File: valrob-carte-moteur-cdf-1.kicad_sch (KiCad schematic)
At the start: 50 parts, among them J1 USB_C_Receptacle_USB2.0_14P, J2 Conn_01x02, J3 Conn_01x02, J4 Conn_01x04_Pin, J5 Conn_01x08, J6 Conn_01x02, J7 Conn_01x02, J8 Conn_01x08, J9 Conn_01x04_Pin, SW1 SW_Push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

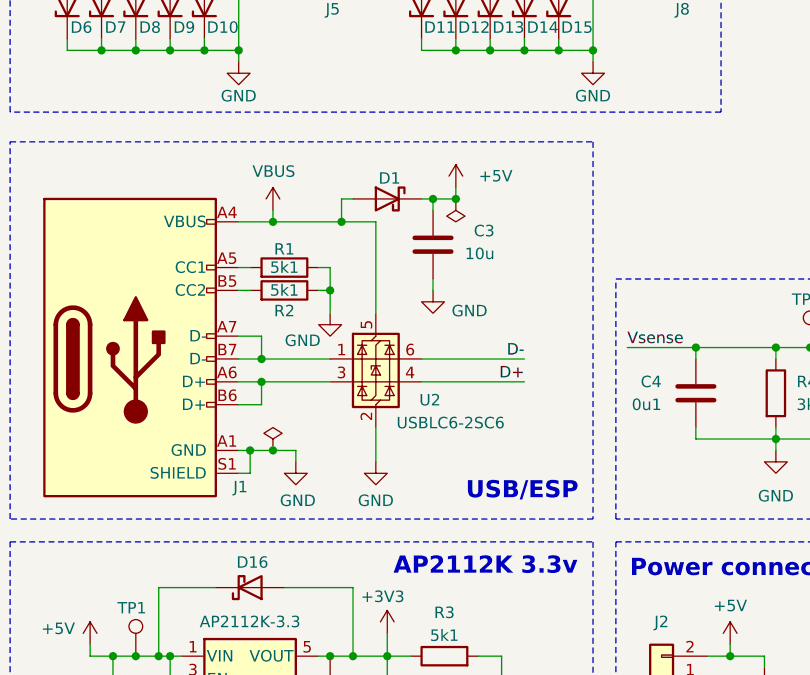
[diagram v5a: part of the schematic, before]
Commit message: switch ST usb ESD to H5VU10U tvs diodes
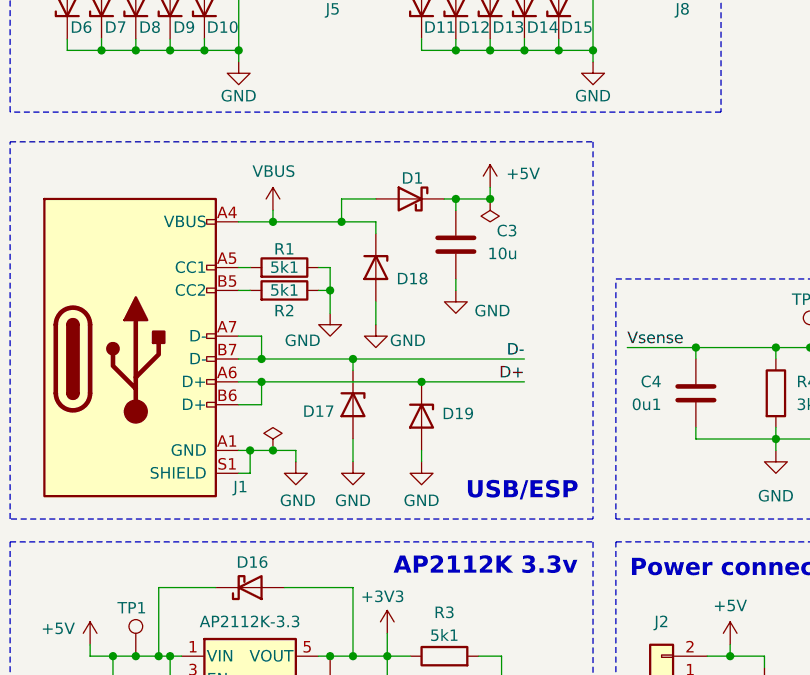
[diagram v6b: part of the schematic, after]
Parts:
- removed U2: USBLC6-2SC6, Package_TO_SOT_SMD:SOT-23-6, symbol Power_Protection:USBLC6-2SC6
- added D17, D18, D19: H5VU10U, Pers:Diode_DFN1006, symbol Pers:H5VU10U
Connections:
- net D+: now also J1.A6 (D+), J1.B6 (D+), D19.1 (K)
- net D-: now also J1.A7 (D-), J1.B7 (D-), D17.1 (K)
- net GND: now also D17.2 (A), D18.2 (A), D19.2 (A)
- net VBUS: now also D18.1 (K)
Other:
- moved on the sheet: C3, D1

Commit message: pcb(silkscreeen): improvements
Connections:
- net +12V: now also C4.1, D4.1 (K), TP3.1
- net Vsense: no longer C4.1, D4.1 (K), TP3.1
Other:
- moved on the sheet: C4, D4, R4, R6, TP3

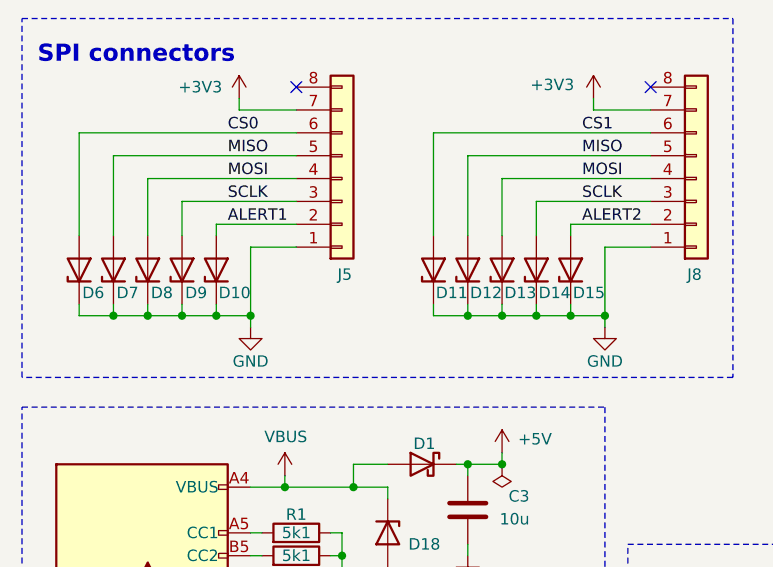
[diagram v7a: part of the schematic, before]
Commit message: fix spi connectors TVS diodes polarity
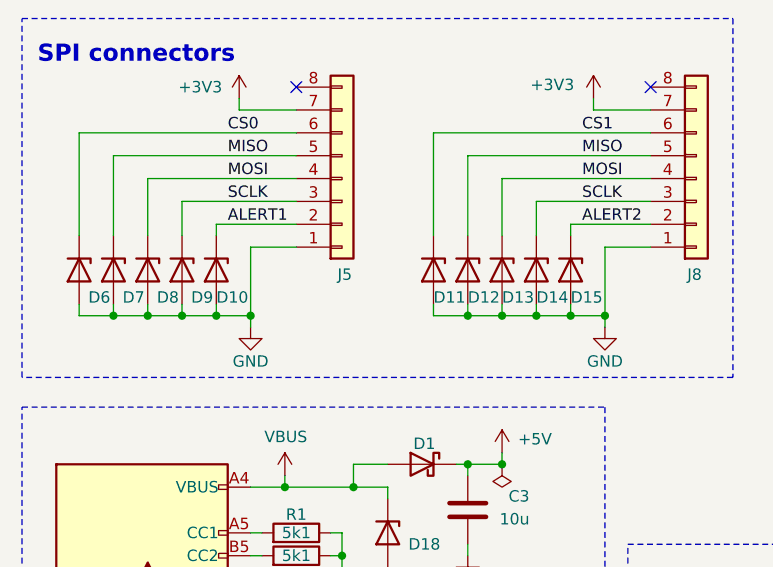
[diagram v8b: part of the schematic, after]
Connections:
- net ALERT1: now also D10.1 (K); no longer D10.2 (A)
- net ALERT2: now also D15.1 (K); no longer D15.2 (A)
- net CS0: now also D6.1 (K); no longer D6.2 (A)
- net CS1: now also D11.1 (K); no longer D11.2 (A)
- net GND: now also D10.2 (A), D11.2 (A), D12.2 (A), D13.2 (A), D14.2 (A), D15.2 (A), D6.2 (A), D7.2 (A), D8.2 (A), D9.2 (A); no longer D10.1 (K), D11.1 (K), D12.1 (K), D13.1 (K), D14.1 (K), D15.1 (K), D6.1 (K), D7.1 (K), D8.1 (K), D9.1 (K)
- net MISO: now also D12.1 (K), D7.1 (K); no longer D12.2 (A), D7.2 (A)
- net MOSI: now also D13.1 (K), D8.1 (K); no longer D13.2 (A), D8.2 (A)
- net SCLK: now also D14.1 (K), D9.1 (K); no longer D14.2 (A), D9.2 (A)
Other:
- moved on the sheet: D10, D11, D12, D13, D14, D15, D6, D7, D8, D9
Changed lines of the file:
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@@
 	(wire
 		(pts
-			(xy 40.64 102.87) (xy 40.64 110.49)
-		)
-		(stroke
-			(width 0)
-			(type default)
-		)
-	)
-	(wire
-		(pts
 			(xy 55.88 129.54) (xy 52.07 129.54)
 		)
@@
 	(wire
 		(pts
+			(xy 40.64 102.87) (xy 40.64 110.49)
+		)
+		(stroke
+			(width 0)
+			(type default)
+		)
+	)
+	(wire
+		(pts
 			(xy 26.67 187.96) (xy 26.67 189.23)
 		)
@@
 	(symbol
 		(lib_id "Pers:H5VU10U")
-		(at 68.58 105.41 90)
+		(at 68.58 105.41 270)
 		(unit 1)
 		(exclude_from_sim no)
@@
 		(dnp no)
 		(property "Reference" "D13"
-			(at 72.39 107.95 90)
+			(at 68.58 108.458 90)
 			(effects
 				(font
@@
 		)
 		(property "Value" "H5VU10U"
-			(at 66.04 104.1401 90)
+			(at 71.12 106.6799 90)
 			(effects
 				(font
@@
 		)
 		(property "Footprint" "Pers:Diode_DFN1006"
-			(at 73.025 105.41 0)
+			(at 64.135 105.41 0)
 			(effects
 				(font
@@
 	(symbol
 		(lib_id "Pers:H5VU10U")
-		(at 21.59 105.41 90)
+		(at 21.59 105.41 270)
 		(unit 1)
 		(exclude_from_sim no)
@@
 		(dnp no)
 		(property "Reference" "D6"
-			(at 24.384 107.95 90)
+			(at 22.606 108.458 90)
 			(effects
 				(font
@@
 		)
 		(property "Value" "H5VU10U"
-			(at 19.05 104.1401 90)
+			(at 24.13 106.6799 90)
 			(effects
 				(font
@@
 		)
 		(property "Footprint" "Pers:Diode_DFN1006"
-			(at 26.035 105.41 0)
+			(at 17.145 105.41 0)
 			(effects
 				(font
@@
 	(symbol
 		(lib_id "Pers:H5VU10U")
-		(at 64.77 105.41 90)
+		(at 64.77 105.41 270)
 		(unit 1)
 		(exclude_from_sim no)
@@
 		(dnp no)
 		(property "Reference" "D12"
-			(at 68.58 107.95 90)
+			(at 64.77 108.458 90)
 			(effects
 				(font
@@
 		)
 		(property "Value" "H5VU10U"
-			(at 62.23 104.1401 90)
+			(at 67.31 106.6799 90)
 			(effects
 				(font
@@
 		)
 		(property "Footprint" "Pers:Diode_DFN1006"
-			(at 69.215 105.41 0)
+			(at 60.325 105.41 0)
 			(effects
 				(font
@@
 	(symbol
 		(lib_id "Pers:H5VU10U")
-		(at 29.21 105.41 90)
+		(at 29.21 105.41 270)
 		(unit 1)
 		(exclude_from_sim no)
@@
 		(dnp no)
 		(property "Reference" "D8"
-			(at 32.004 107.95 90)
+			(at 30.226 108.458 90)
 			(effects
 				(font
@@
 		)
 		(property "Value" "H5VU10U"
-			(at 26.67 104.1401 90)
+			(at 31.75 106.6799 90)
 			(effects
 				(font
@@
 		)
 		(property "Footprint" "Pers:Diode_DFN1006"
-			(at 33.655 105.41 0)
+			(at 24.765 105.41 0)
 			(effects
 				(font
@@
 	(symbol
 		(lib_id "Pers:H5VU10U")
-		(at 25.4 105.41 90)
+		(at 25.4 105.41 270)
 		(unit 1)
 		(exclude_from_sim no)
@@
 		(dnp no)
 		(property "Reference" "D7"
-			(at 28.194 107.95 90)
+			(at 26.416 108.458 90)
 			(effects
 				(font
@@
 		)
 		(property "Value" "H5VU10U"
-			(at 22.86 104.1401 90)
+			(at 27.94 106.6799 90)
 			(effects
 				(font
@@
 		)
 		(property "Footprint" "Pers:Diode_DFN1006"
-			(at 29.845 105.41 0)
+			(at 20.955 105.41 0)
 			(effects
 				(font
@@
 	(symbol
 		(lib_id "Pers:H5VU10U")
-		(at 33.02 105.41 90)
+		(at 33.02 105.41 270)
 		(unit 1)
 		(exclude_from_sim no)
@@
 		(dnp no)
 		(property "Reference" "D9"
-			(at 35.814 107.95 90)
+			(at 34.036 108.458 90)
 			(effects
 				(font
@@
 		)
 		(property "Value" "H5VU10U"
-			(at 30.48 104.1401 90)
+			(at 35.56 106.6799 90)
 			(effects
 				(font
@@
 		)
 		(property "Footprint" "Pers:Diode_DFN1006"
-			(at 37.465 105.41 0)
+			(at 28.575 105.41 0)
 			(effects
 				(font
@@
 	(symbol
 		(lib_id "Pers:H5VU10U")
-		(at 72.39 105.41 90)
+		(at 72.39 105.41 270)
 		(unit 1)
 		(exclude_from_sim no)
@@
 		(dnp no)
 		(property "Reference" "D14"
-			(at 76.2 107.95 90)
+			(at 72.39 108.458 90)
 			(effects
 				(font
@@
 		)
 		(property "Value" "H5VU10U"
-			(at 69.85 104.1401 90)
+			(at 74.93 106.6799 90)
 			(effects
 				(font
@@
 		)
 		(property "Footprint" "Pers:Diode_DFN1006"
-			(at 76.835 105.41 0)
+			(at 67.945 105.41 0)
 			(effects
 				(font
@@
 	(symbol
 		(lib_id "Pers:H5VU10U")
-		(at 60.96 105.41 90)
+		(at 60.96 105.41 270)
 		(unit 1)
 		(exclude_from_sim no)
@@
 		(dnp no)
 		(property "Reference" "D11"
-			(at 64.77 107.95 90)
+			(at 60.96 108.458 90)
 			(effects
 				(font
@@
 		)
 		(property "Value" "H5VU10U"
-			(at 58.42 104.1401 90)
+			(at 63.5 106.6799 90)
 			(effects
 				(font
@@
 		)
 		(property "Footprint" "Pers:Diode_DFN1006"
-			(at 65.405 105.41 0)
+			(at 56.515 105.41 0)
 			(effects
 				(font
@@
 	(symbol
 		(lib_id "Pers:H5VU10U")
-		(at 76.2 105.41 90)
+		(at 76.2 105.41 270)
 		(unit 1)
 		(exclude_from_sim no)
@@
 		(dnp no)
 		(property "Reference" "D15"
-			(at 80.01 107.95 90)
+			(at 76.2 108.458 90)
 			(effects
 				(font
@@
 		)
 		(property "Value" "H5VU10U"
-			(at 73.66 104.1401 90)
+			(at 78.74 106.6799 90)
 			(effects
 				(font
@@
 		)
 		(property "Footprint" "Pers:Diode_DFN1006"
-			(at 80.645 105.41 0)
+			(at 71.755 105.41 0)
 			(effects
 				(font
@@
 	(symbol
 		(lib_id "Pers:H5VU10U")
-		(at 36.83 105.41 90)
+		(at 36.83 105.41 270)
 		(unit 1)
 		(exclude_from_sim no)
@@
 		(dnp no)
 		(property "Reference" "D10"
-			(at 40.64 107.95 90)
+			(at 36.83 108.458 90)
 			(effects
 				(font
@@
 		)
 		(property "Value" "H5VU10U"
-			(at 34.29 104.1401 90)
+			(at 39.37 106.6799 90)
 			(effects
 				(font
@@
 		)
 		(property "Footprint" "Pers:Diode_DFN1006"
-			(at 41.275 105.41 0)
+			(at 32.385 105.41 0)
 			(effects
 				(font
